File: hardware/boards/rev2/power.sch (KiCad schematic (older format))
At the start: 108 parts, among them CON1 BARREL_JACK, U26 L7981-fmcw3-rescue, U27 L7981-fmcw3-rescue, U28 L7981-fmcw3-rescue, U29 LP2985A-10DBVR, U30 TPS7A91, U31 TPS7A91, U32 TPS7A91, U33 LP5907MFX-3.0, U34 TPS7A91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

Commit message: reorganize schematic
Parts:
- removed U26, U27, U28: L7981-fmcw3-rescue, Package_SO:HSOP-8-1EP_3.9x4.9mm_P1.27mm_EP2.41x3.1mm, symbol fmcw-rescue:L7981-fmcw3-rescue
- added U26, U27, U28: L7980, fmcw:HSOP-8-1EP_3.9x4.9mm_P1.27mm_EP2.3x2.3mm_ThermalVias, symbol fmcw:L7980
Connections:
- net 12V: now also U26.3 (EN), U26.8 (VCC), U27.3 (EN), U27.8 (VCC), U28.8 (VCC)
- net GND: now also U26.7 (GND), U26.9 (EP), U27.7 (GND), U27.9 (EP), U28.7 (GND), U28.9 (EP)
- net SYNC: now also U26.2 (SYNC), U27.2 (SYNC)
- net at D3.1 (K), L6.1: now also U27.1 (OUT)
- net at C117.2, C126.2, C179.2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: now also U27.5 (FB)
- net at C126.1, R57.1: now also U27.4 (COMP)
- net at R55.1: now also U27.6 (FSW)
- net at C111.2, C125.2, C155.2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: now also U26.5 (FB)
- net at D4.1 (K), L5.1: now also U26.1 (OUT)
- net at C125.1, R56.1: now also U26.4 (COMP)
- net at R54.1: now also U26.6 (FSW)
- net at C143.2, C146.2, C158.2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: now also U28.5 (FB)
- net at D5.1 (K), L7.1: now also U28.1 (OUT)
- net at R85.2: now also U28.2 (SYNC)
- net at R60.1, R83.1: now also U28.3 (EN)
- net at C146.1, R84.1: now also U28.4 (COMP)
- net at R59.1: now also U28.6 (FSW)
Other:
- note added: "1,000 (538) mA"
- note added: "1,105 (525) mA"
- note added: "15 mA"
- note added: "27 (10) mA [85% eff.]"
- note added: "277 (97) mA"
- note added: "3 mA"
- note added: "326 (179) mA [92% eff.]"
- note added: "573 (272) mA [90% eff.]"
- note added: "944 (479) mA"
- moved on the sheet: C111, C117, C125, C126, C143, C146, C155, C167, C169, C170, C171, C173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

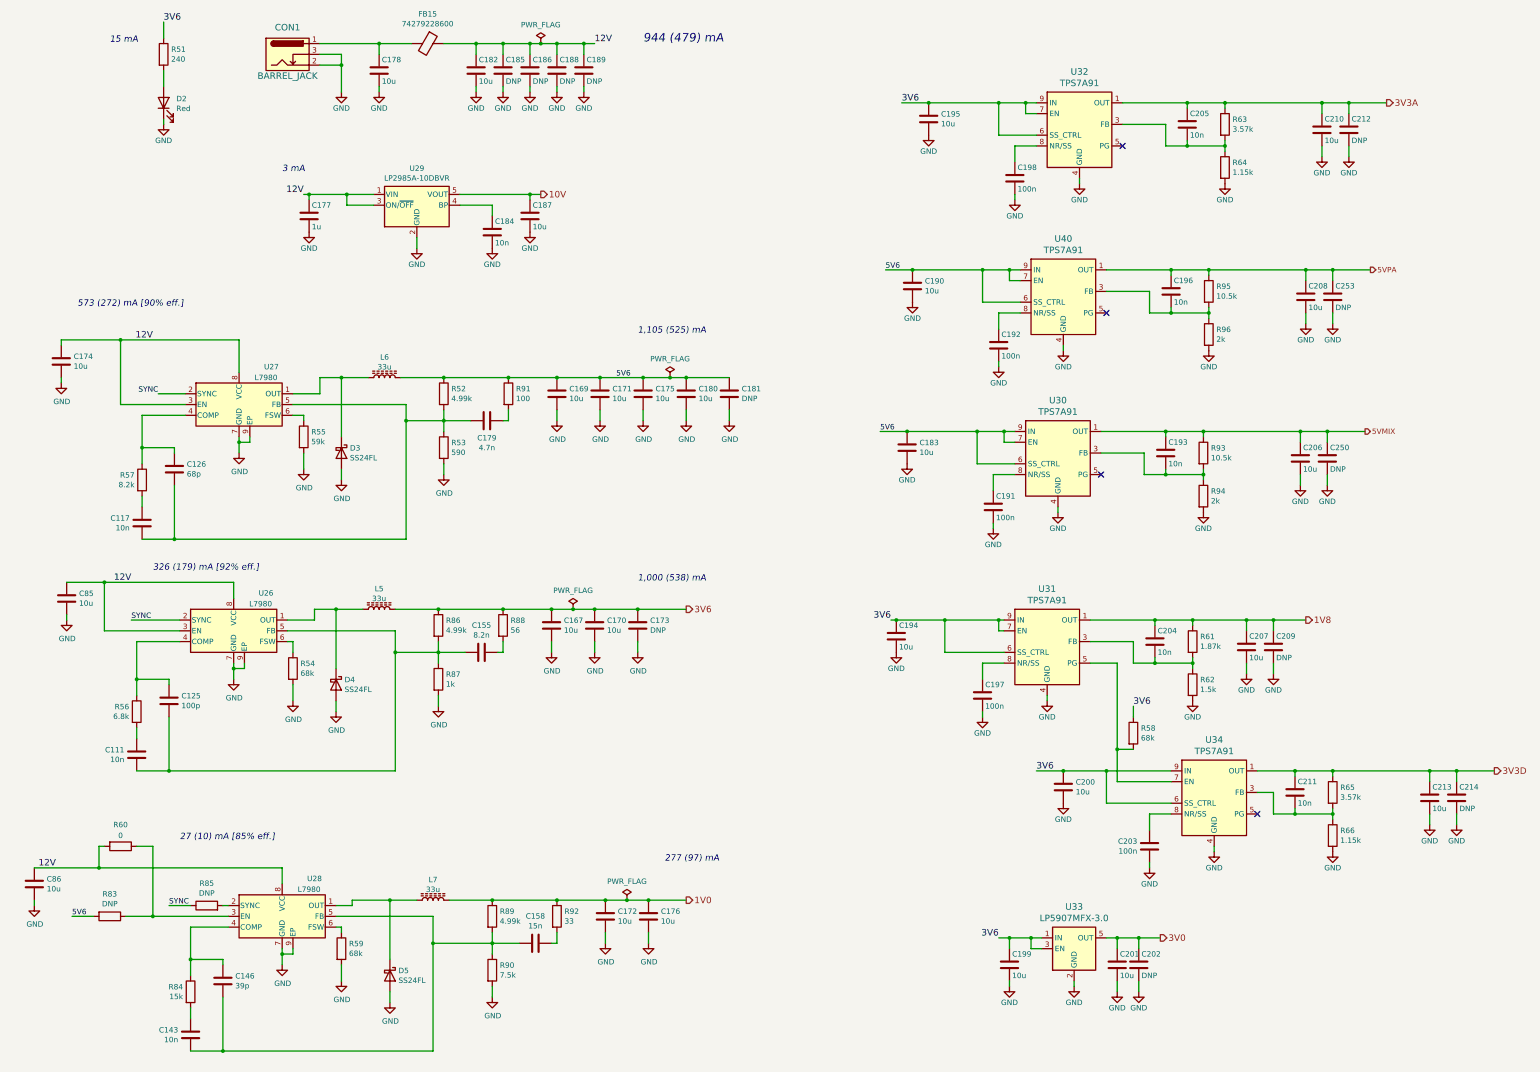
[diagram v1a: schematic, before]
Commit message: revert to kicad v5 for pcb gen
V6 contains a few bugs and a V6 board cannot be edited with V5.
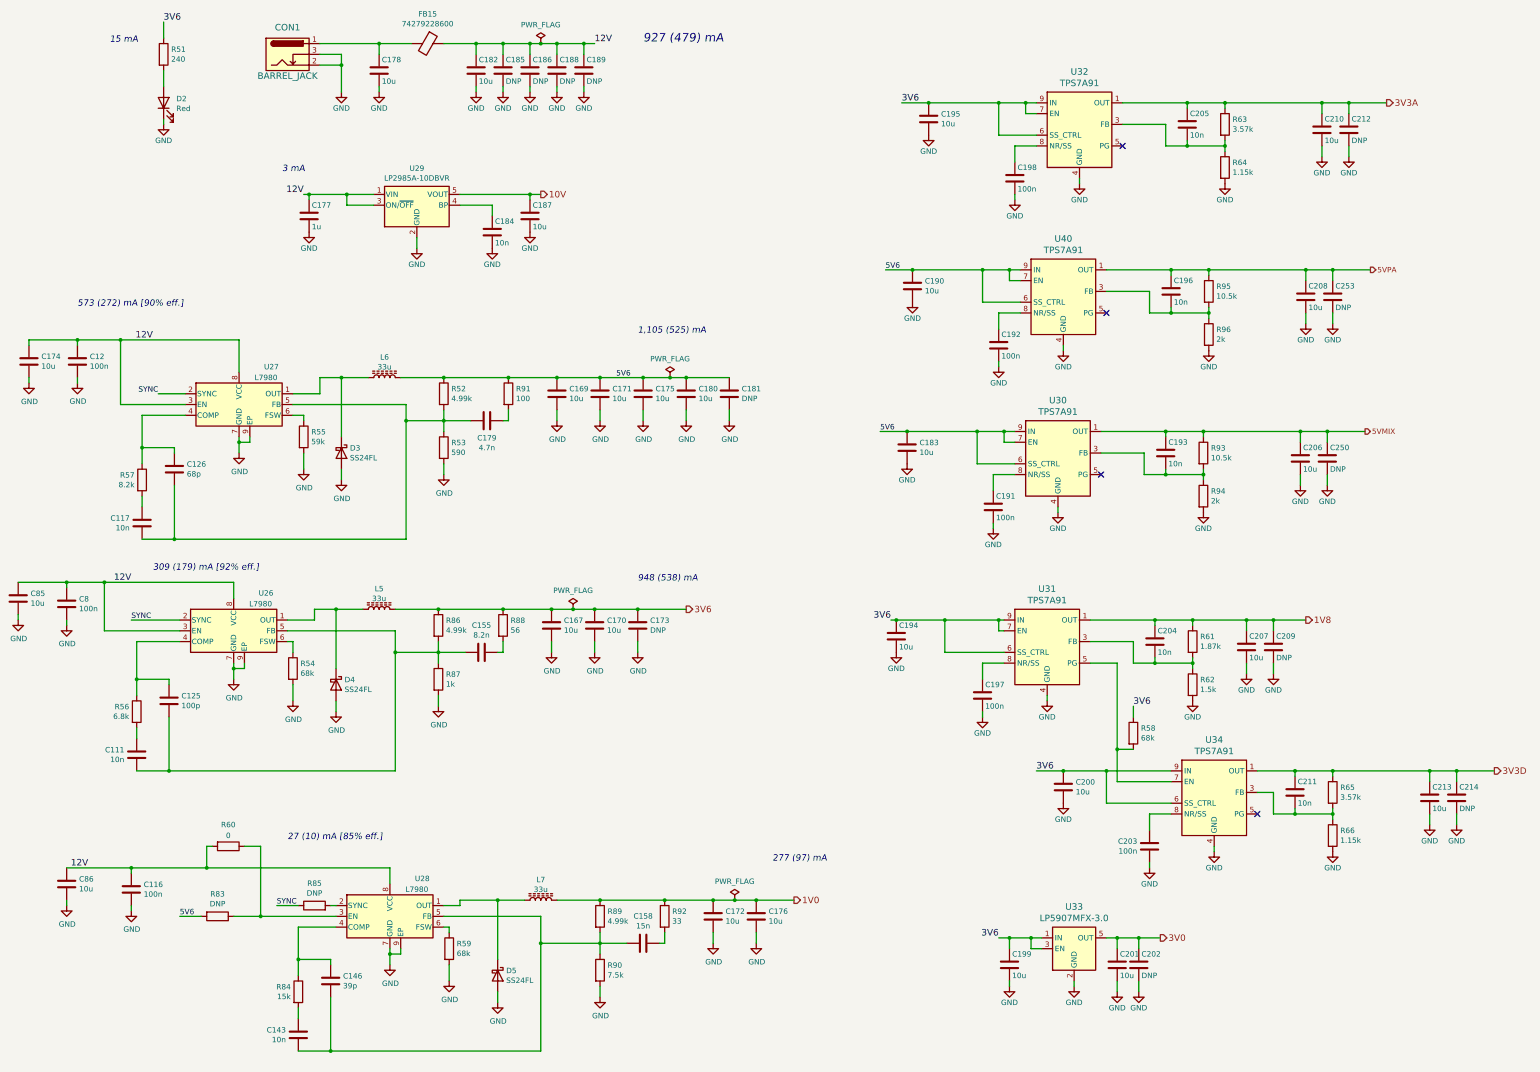
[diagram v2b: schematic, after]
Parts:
- added C116, C12, C8: 100n, Capacitor_SMD:C_0402_1005Metric, symbol Device:C
- D3, D4, D5: footprint fmcw:SOD-123F -> Diode_SMD:D_SOD-123F
- L5, L6: footprint Inductor_SMD:L_Bourns_SRR1210A -> Inductor_SMD:L_Wuerth_HCI-1365; MFN SRR1210A-330M -> 7443551331
- L7: footprint fmcw:SRR6040A -> fmcw_v5:SRR6040A
- U26, U27, U28: footprint fmcw:HSOP-8-1EP_3.9x4.9mm_P1.27mm_EP2.3x2.3mm_ThermalVias -> fmcw_v5:HSOP-8-1EP_3.9x4.9mm_P1.27mm_EP2.3x2.3mm_ThermalVias
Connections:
- net 12V: now also C116.1, C12.1, C8.1
- net GND: now also C116.2, C12.2, C8.2
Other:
- note added: "309 (179) mA [92% eff.]"
- note added: "927 (479) mA"
- note added: "948 (538) mA"
- note removed: "1,000 (538) mA"
- note removed: "326 (179) mA [92% eff.]"
- note removed: "944 (479) mA"
- moved on the sheet: C143, C146, C158, C172, C174, C176, C85, C86, D5, L7, R59, R60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

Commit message: finish placement and routing
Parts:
- L7: footprint fmcw_v5:SRR6040A -> fmcw_v5:L_Bourns_SRR6040A
- U30, U31, U32, U34, U40: footprint Package_DFN_QFN:Texas_S-PDSO-N10_EP1.2x2mm -> Package_DFN_QFN:Texas_S-PDSO-N10_EP1.2x2mm_ThermalVias
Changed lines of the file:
@@
 F 0 "L7" V 5640 9400 50  0000 C CNN
 F 1 "33u" V 5549 9400 50  0000 C CNN
-F 2 "fmcw_v5:SRR6040A" H 5450 9400 60  0001 C CNN
+F 2 "fmcw_v5:L_Bourns_SRR6040A" H 5450 9400 60  0001 C CNN
 F 3 "" H 5450 9400 60  0001 C CNN
 F 4 "SRR6040A-330M" H -250 4200 50  0001 C CNN "MFN"
@@
 F 0 "U31" H 10150 7689 60  0000 C CNN
 F 1 "TPS7A91" H 10150 7583 60  0000 C CNN
-F 2 "Package_DFN_QFN:Texas_S-PDSO-N10_EP1.2x2mm" H 10200 7200 60  0001 C CNN
+F 2 "Package_DFN_QFN:Texas_S-PDSO-N10_EP1.2x2mm_ThermalVias" H 10200 7200 60  0001 C CNN
 F 3 "" H 10200 7200 60  0001 C CNN
 F 4 "TPS7A9101DSKT" H -250 1850 50  0001 C CNN "MFN"
@@
 F 0 "U30" H 10250 5939 60  0000 C CNN
 F 1 "TPS7A91" H 10250 5833 60  0000 C CNN
-F 2 "Package_DFN_QFN:Texas_S-PDSO-N10_EP1.2x2mm" H 10300 5450 60  0001 C CNN
+F 2 "Package_DFN_QFN:Texas_S-PDSO-N10_EP1.2x2mm_ThermalVias" H 10300 5450 60  0001 C CNN
 F 3 "" H 10300 5450 60  0001 C CNN
 F 4 "TPS7A9101DSKT" H -200 3050 50  0001 C CNN "MFN"
@@
 F 0 "U40" H 10300 4439 60  0000 C CNN
 F 1 "TPS7A91" H 10300 4333 60  0000 C CNN
-F 2 "Package_DFN_QFN:Texas_S-PDSO-N10_EP1.2x2mm" H 10350 3950 60  0001 C CNN
+F 2 "Package_DFN_QFN:Texas_S-PDSO-N10_EP1.2x2mm_ThermalVias" H 10350 3950 60  0001 C CNN
 F 3 "" H 10350 3950 60  0001 C CNN
 F 4 "TPS7A9101DSKT" H -150 1550 50  0001 C CNN "MFN"
@@
 F 0 "U32" H 10450 2889 60  0000 C CNN
 F 1 "TPS7A91" H 10450 2783 60  0000 C CNN
-F 2 "Package_DFN_QFN:Texas_S-PDSO-N10_EP1.2x2mm" H 10500 2400 60  0001 C CNN
+F 2 "Package_DFN_QFN:Texas_S-PDSO-N10_EP1.2x2mm_ThermalVias" H 10500 2400 60  0001 C CNN
 F 3 "" H 10500 2400 60  0001 C CNN
 F 4 "TPS7A9101DSKT" H 0   0   50  0001 C CNN "MFN"
@@
 F 0 "U34" H 11700 9089 60  0000 C CNN
 F 1 "TPS7A91" H 11700 8983 60  0000 C CNN
-F 2 "Package_DFN_QFN:Texas_S-PDSO-N10_EP1.2x2mm" H 11750 8600 60  0001 C CNN
+F 2 "Package_DFN_QFN:Texas_S-PDSO-N10_EP1.2x2mm_ThermalVias" H 11750 8600 60  0001 C CNN
 F 3 "" H 11750 8600 60  0001 C CNN
 F 4 "TPS7A9101DSKT" H 1250 6200 50  0001 C CNN "MFN"
